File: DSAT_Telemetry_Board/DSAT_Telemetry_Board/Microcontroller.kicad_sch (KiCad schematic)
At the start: 15 parts

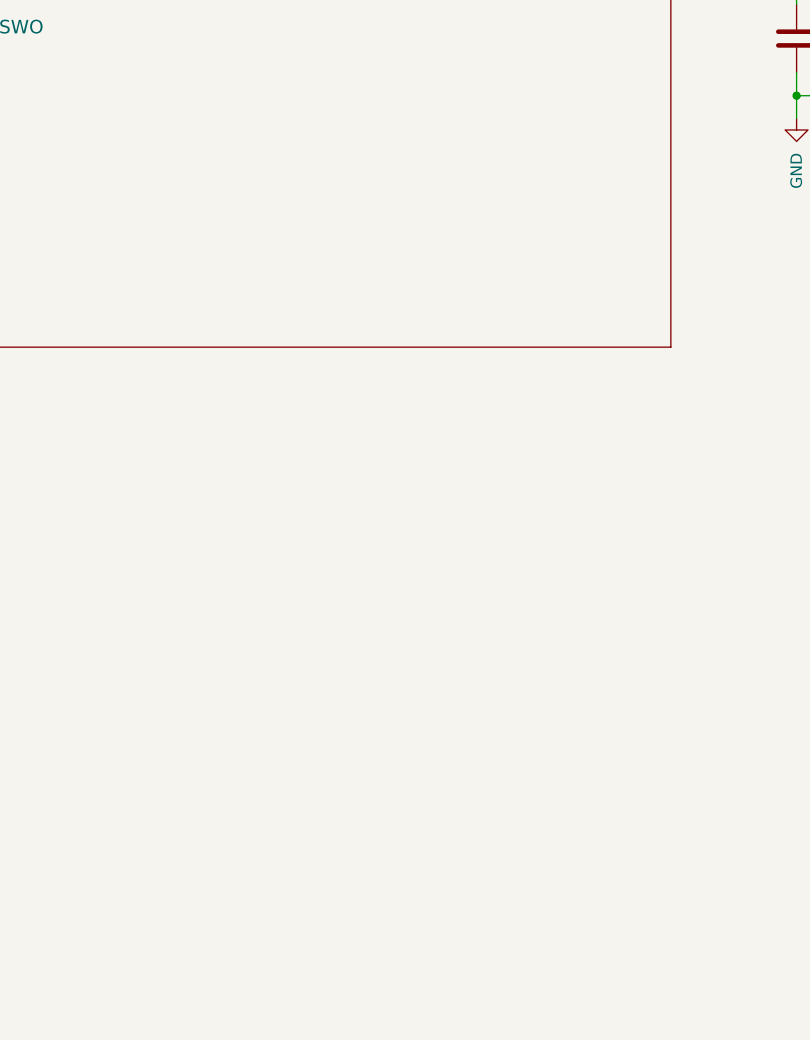
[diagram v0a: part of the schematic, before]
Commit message: antenna matching netowrks for Rx and Tx added partially
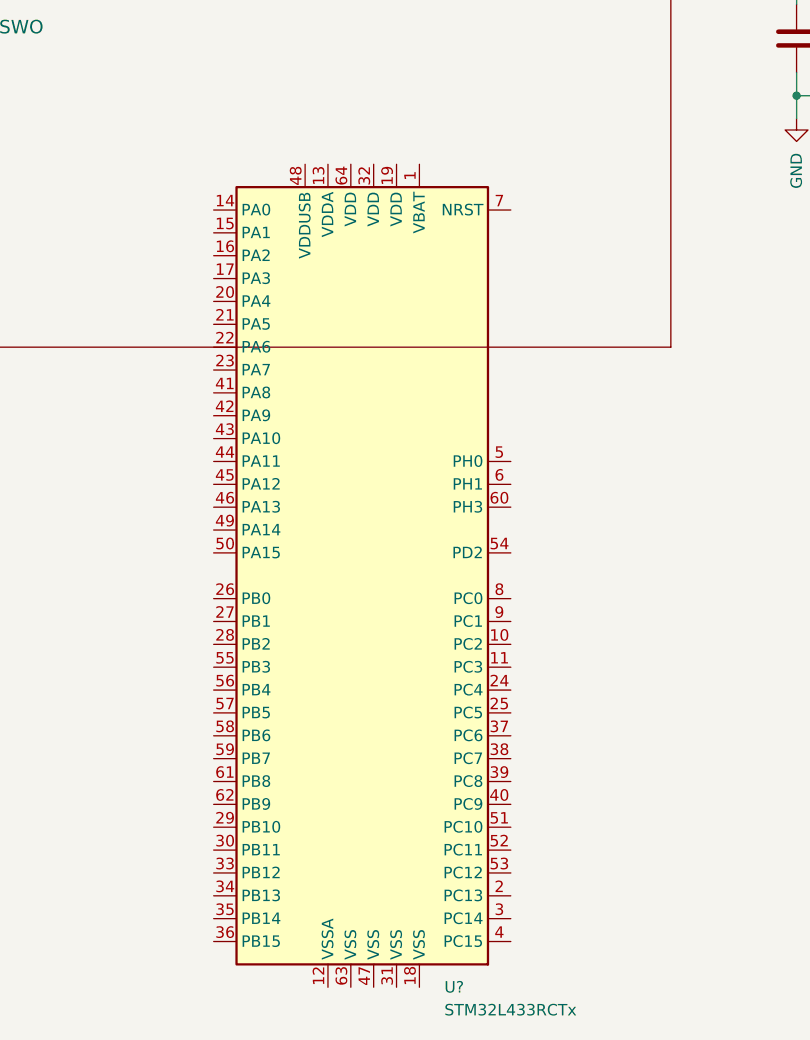
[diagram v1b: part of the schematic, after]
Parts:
- added U?: STM32L433RCTx, Package_QFP:LQFP-64_10x10mm_P0.5mm, symbol MCU_ST_STM32L4:STM32L433RCTx
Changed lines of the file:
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@@
     (pin "2")
+  )
+  (symbol (lib_id "MCU_ST_STM32L4:STM32L433RCTx") (at 176.53 165.1 0) (mirror y) (unit 1)
+    (in_bom yes) (on_board yes) (fields_autoplaced)
+    (property "Reference" "U?" (id 0) (at 186.9187 210.82 0)
+      (effects (font (size 1.27 1.27)) (justify right))
+    )
+    (property "Value" "STM32L433RCTx" (id 1) (at 186.9187 213.36 0)
+      (effects (font (size 1.27 1.27)) (justify right))
+    )
+    (property "Footprint" "Package_QFP:LQFP-64_10x10mm_P0.5mm" (id 2) (at 191.77 208.28 0)
+      (effects (font (size 1.27 1.27)) (justify right) hide)
+    )
+    (property "Datasheet" "http://www.st.com/st-web-ui/static/active/en/resource/technical/document/datasheet/DM00257192.pdf" (id 3) (at 176.53 165.1 0)
+      (effects (font (size 1.27 1.27)) hide)
+    )
+    (pin "1")
+    (pin "10")
+    (pin "11")
+    (pin "12")
+    (pin "13")
+    (pin "14")
+    (pin "15")
+    (pin "16")
+    (pin "17")
+    (pin "18")
+    (pin "19")
+    (pin "2")
+    (pin "20")
+    (pin "21")
+    (pin "22")
+    (pin "23")
+    (pin "24")
+    (pin "25")
+    (pin "26")
+    (pin "27")
+    (pin "28")
+    (pin "29")
+    (pin "3")
+    (pin "30")
+    (pin "31")
+    (pin "32")
+    (pin "33")
+    (pin "34")
+    (pin "35")
+    (pin "36")
+    (pin "37")
+    (pin "38")
+    (pin "39")
+    (pin "4")
+    (pin "40")
+    (pin "41")
+    (pin "42")
+    (pin "43")
+    (pin "44")
+    (pin "45")
+    (pin "46")
+    (pin "47")
+    (pin "48")
+    (pin "49")
+    (pin "5")
+    (pin "50")
+    (pin "51")
+    (pin "52")
+    (pin "53")
+    (pin "54")
+    (pin "55")
+    (pin "56")
+    (pin "57")
+    (pin "58")
+    (pin "59")
+    (pin "6")
+    (pin "60")
+    (pin "61")
+    (pin "62")
+    (pin "63")
+    (pin "64")
+    (pin "7")
+    (pin "8")
+    (pin "9")
   )
   (symbol (lib_id "power:+3.3V") (at 95.25 93.98 0) (mirror y) (unit 1)
@@
     (pin "6")
     (pin "7")
-    (pin "1")
-    (pin "23")
-    (pin "24")
-    (pin "35")
-    (pin "36")
-    (pin "47")
-    (pin "48")
-    (pin "8")
-    (pin "9")
   )
   (symbol (lib_id "power:GND") (at 226.06 114.3 0) (unit 1)

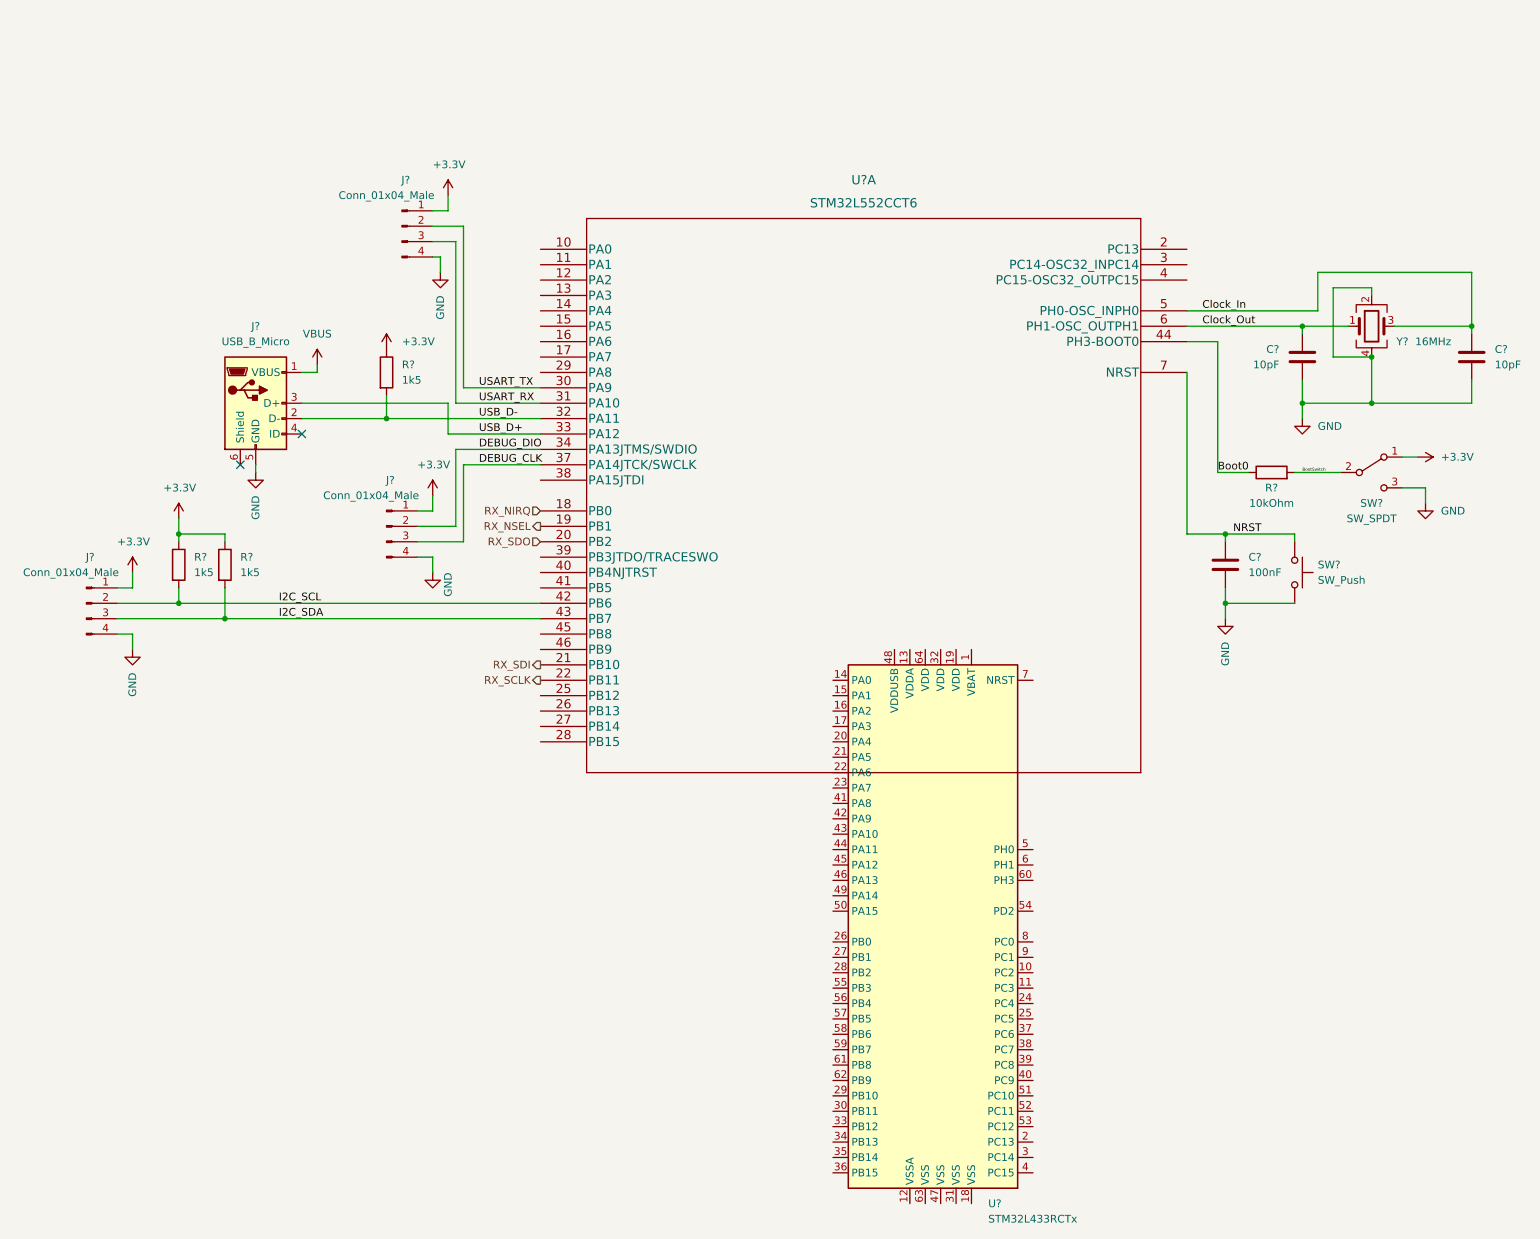
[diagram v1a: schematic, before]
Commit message: change to proper mcu and various schematic changes and additions
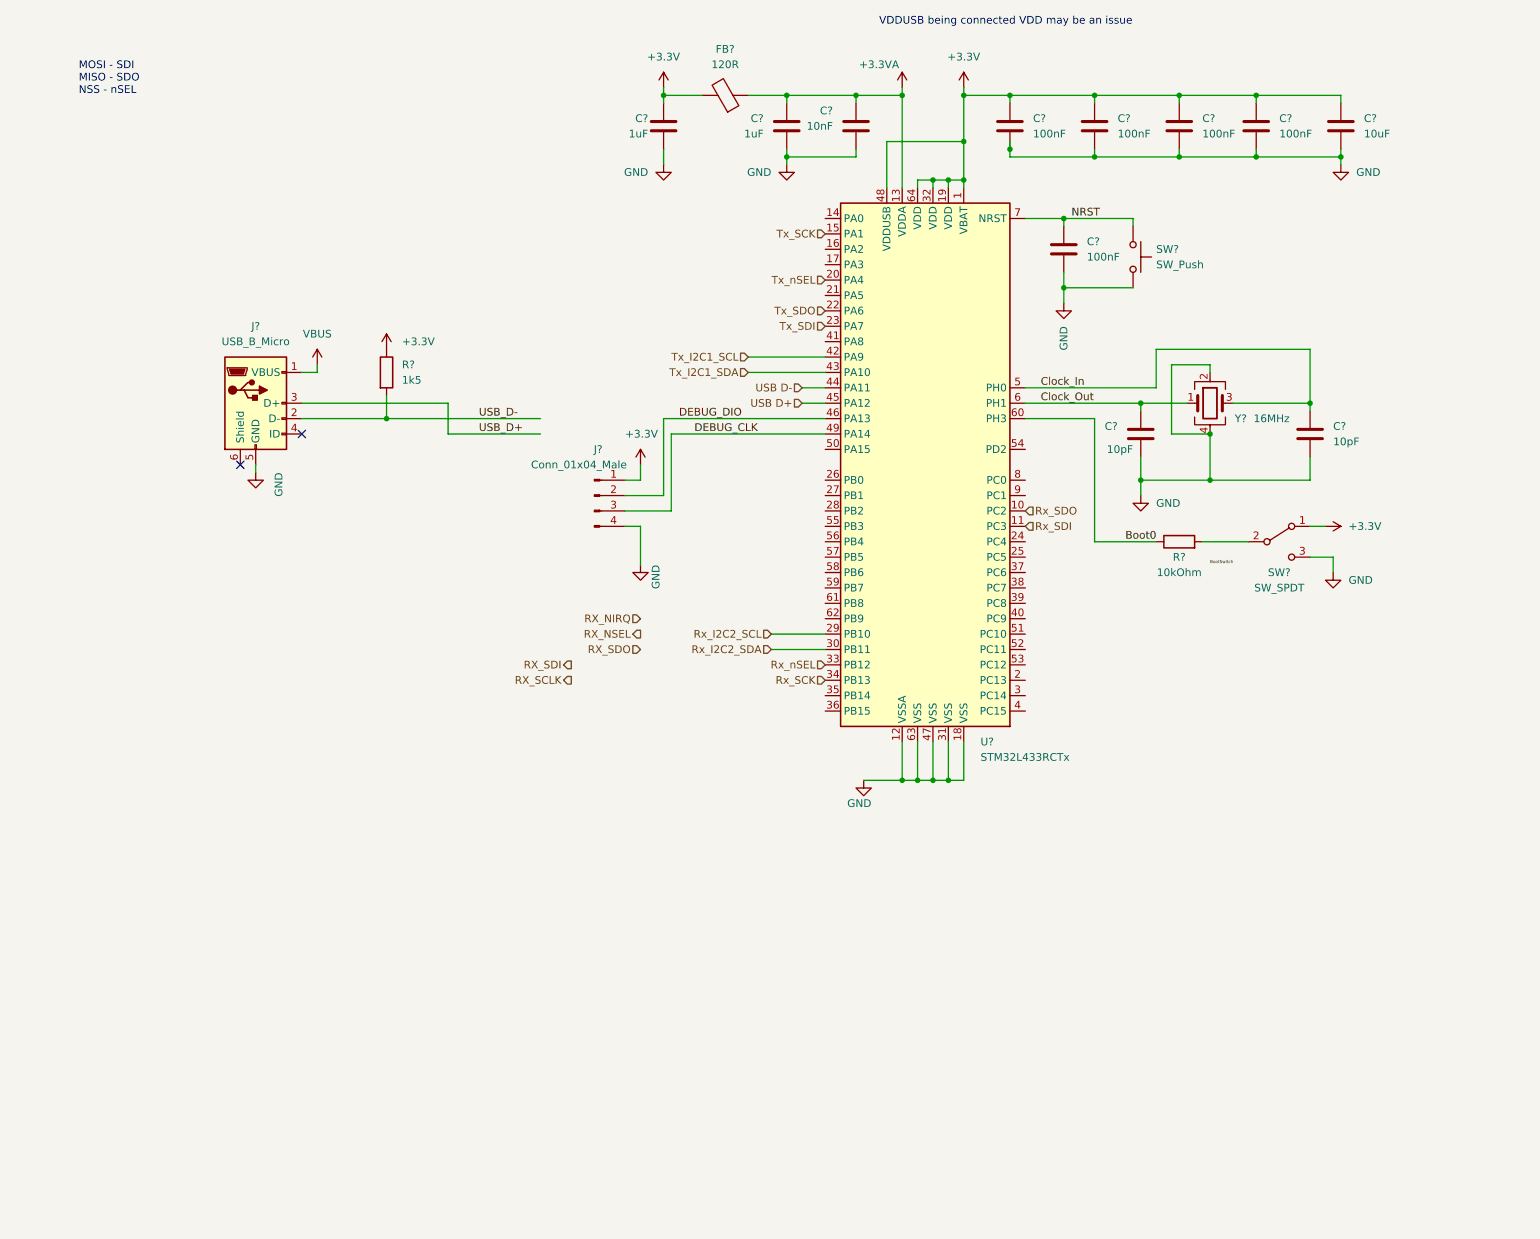
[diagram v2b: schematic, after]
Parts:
- removed J? (x2): Conn_01x04_Male, symbol Connector:Conn_01x04_Male
- removed R? (x2): 1k5, symbol Device:R
- removed U?: STM32L552CCT6, LQFP-48, symbol STM32L5:STM32L552CCT6
- added C? (x2): 1uF, symbol Device:C
- added C? (x4): 100nF, symbol Device:C
- added C?: 10uF, symbol Device:C
- added C?: 10nF, symbol Device:C
- added FB?: 120R, symbol Device:FerriteBead
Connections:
- net +3.3V: now also U?.1 (VBAT), U?.19 (VDD), U?.32 (VDD), U?.48 (VDDUSB), U?.64 (VDD), C?.1, C?.1, C?.1, C?.1, C?.1, C?.1, FB?.2
- net Boot0: now also U?.60 (PH3)
- net BootSwitch: no longer R?.2, SW?.2 (B)
- net Clock_In: now also U?.5 (PH0)
- net Clock_Out: now also U?.6 (PH1)
- net DEBUG_CLK: now also U?.49 (PA14)
- net DEBUG_DIO: now also U?.46 (PA13)
- net GND: now also U?.12 (VSSA), U?.18 (VSS), U?.31 (VSS), U?.47 (VSS), U?.63 (VSS), C?.2, C?.2, C?.2, C?.2, C?.2, C?.2, C?.2, C?.2
- net NRST: now also U?.7 (NRST)
- net Rx_SDO: now reaches U?.10 (PC2)
- net Rx_SDI: now reaches U?.11 (PC3)
- net +3.3VA: now reaches U?.13 (VDDA)
- net +3.3VA: now also C?.1, C?.1, FB?.1
- net Tx_SCK: now reaches U?.15 (PA1)
- net Tx_nSEL: now reaches U?.20 (PA4)
- net Tx_SDO: now reaches U?.22 (PA6)
- net Tx_SDI: now reaches U?.23 (PA7)
- net Rx_I2C2_SCL: now reaches U?.29 (PB10)
- net Rx_I2C2_SDA: now reaches U?.30 (PB11)
- net Rx_nSEL: now reaches U?.33 (PB12)
- net Rx_SCK: now reaches U?.34 (PB13)
- net Tx_I2C1_SCL: now reaches U?.42 (PA9)
- net Tx_I2C1_SDA: now reaches U?.43 (PA10)
- net USB D-: now reaches U?.44 (PA11)
- net USB D+: now reaches U?.45 (PA12)
- new net: R?.2, SW?.2 (B)
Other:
- note added: "MOSI - SDI MISO - SDO NSS - nSEL"
- note added: "VDDUSB being connected VDD may be an issue"
- moved on the sheet: C?, J?, R?, SW?, U?, Y?

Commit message: Updated Microcontroller Pinout Names
Updated Names
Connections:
- net Rx_SDI is gone; now on net RX_SDI: U?.11 (PC3)
- net Rx_SDO is gone; now on net RX_SDO: U?.10 (PC2)
- net Rx_I2C2_SCL renamed I2C2_SCL
- net Rx_I2C2_SDA renamed I2C2_SDA
- net Rx_SCK renamed RX_SCK
- net Rx_nSEL renamed RX_~{SEL}
- net Tx_I2C1_SCL renamed I2C1_SCL
- net Tx_I2C1_SDA renamed I2C1_SDA
- net Tx_SCK renamed TX_SCK
- net Tx_SDI renamed TX_SDI
- net Tx_SDO renamed TX_SDO
- net Tx_nSEL renamed TX_~{SEL}
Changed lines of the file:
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@@
     (effects (font (size 1.27 1.27)) (justify left bottom))
   )
-  (hierarchical_label "Rx_SCK" (shape input) (at 160.02 124.46 180)
-    (effects (font (size 1.27 1.27)) (justify right))
-  )
-  (hierarchical_label "RX_SCLK" (shape output) (at 118.11 124.46 180)
+  (hierarchical_label "RX_SCK" (shape input) (at 160.02 124.46 180)
     (effects (font (size 1.27 1.27)) (justify right))
   )
@@
     (effects (font (size 1.27 1.27)) (justify right))
   )
-  (hierarchical_label "Rx_SDI" (shape input) (at 193.04 99.06 0)
+  (hierarchical_label "RX_SDI" (shape input) (at 193.04 99.06 0)
     (effects (font (size 1.27 1.27)) (justify left))
   )
-  (hierarchical_label "Tx_SDI" (shape input) (at 160.02 66.04 180)
+  (hierarchical_label "TX_SDI" (shape input) (at 160.02 66.04 180)
     (effects (font (size 1.27 1.27)) (justify right))
   )
-  (hierarchical_label "Rx_nSEL" (shape input) (at 160.02 121.92 180)
+  (hierarchical_label "RX_~{SEL}" (shape input) (at 160.02 121.92 180)
     (effects (font (size 1.27 1.27)) (justify right))
   )
-  (hierarchical_label "Rx_I2C2_SDA" (shape input) (at 151.13 119.38 180)
+  (hierarchical_label "I2C2_SDA" (shape input) (at 151.13 119.38 180)
     (effects (font (size 1.27 1.27)) (justify right))
   )
-  (hierarchical_label "Tx_I2C1_SCL" (shape input) (at 147.32 71.12 180)
+  (hierarchical_label "I2C1_SCL" (shape input) (at 147.32 71.12 180)
     (effects (font (size 1.27 1.27)) (justify right))
   )
-  (hierarchical_label "Rx_I2C2_SCL" (shape input) (at 151.13 116.84 180)
-    (effects (font (size 1.27 1.27)) (justify right))
-  )
-  (hierarchical_label "RX_SDO" (shape input) (at 129.54 119.38 180)
+  (hierarchical_label "I2C2_SCL" (shape input) (at 151.13 116.84 180)
     (effects (font (size 1.27 1.27)) (justify right))
   )
@@
     (effects (font (size 1.27 1.27)) (justify right))
   )
-  (hierarchical_label "Tx_nSEL" (shape input) (at 160.02 58.42 180)
+  (hierarchical_label "TX_~{SEL}" (shape input) (at 160.02 58.42 180)
     (effects (font (size 1.27 1.27)) (justify right))
   )
-  (hierarchical_label "RX_NIRQ" (shape input) (at 129.54 114.3 180)
+  (hierarchical_label "I2C1_SDA" (shape input) (at 147.32 73.66 180)
     (effects (font (size 1.27 1.27)) (justify right))
   )
-  (hierarchical_label "Tx_I2C1_SDA" (shape input) (at 147.32 73.66 180)
+  (hierarchical_label "TX_SDO" (shape input) (at 160.02 63.5 180)
     (effects (font (size 1.27 1.27)) (justify right))
   )
-  (hierarchical_label "RX_NSEL" (shape output) (at 129.54 116.84 180)
+  (hierarchical_label "TX_SCK" (shape input) (at 160.02 50.8 180)
     (effects (font (size 1.27 1.27)) (justify right))
   )
-  (hierarchical_label "Tx_SDO" (shape input) (at 160.02 63.5 180)
-    (effects (font (size 1.27 1.27)) (justify right))
-  )
-  (hierarchical_label "Tx_SCK" (shape input) (at 160.02 50.8 180)
-    (effects (font (size 1.27 1.27)) (justify right))
-  )
-  (hierarchical_label "Rx_SDO" (shape input) (at 193.04 96.52 0)
+  (hierarchical_label "RX_SDO" (shape input) (at 193.04 96.52 0)
     (effects (font (size 1.27 1.27)) (justify left))
   )
-  (hierarchical_label "RX_SDI" (shape output) (at 118.11 121.92 180)
-    (effects (font (size 1.27 1.27)) (justify right))
-  )
   (symbol (lib_id "power:+3.3V") (at 242.57 99.06 270) (mirror x) (unit 1)
